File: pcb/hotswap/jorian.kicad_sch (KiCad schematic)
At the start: 59 parts, among them J1 USB-C Conn, J2 Ex_Bat, Q1 AO3407, SW1 SW_PUSH, SW10 SW_PUSH, SW11 SW_PUSH, SW12 SW_PUSH, SW13 SW_PUSH, SW14 SW_PUSH, SW15 SW_PUSH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

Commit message: Proper library management
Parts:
- D1, D3: footprint skean:LED_0603_1608Metric_REV -> kbd:LED_0603_1608Metric_REV
- D2: footprint skean:D_SOD-323_HandSoldering_REV -> kbd:D_SOD-323_HandSoldering_REV
- E10, E15, E16, E18, E19, E20, E21, E5: footprint kbd_jorian:edge_conn -> jorian:edge_conn
- G1, G2: footprint kbd:jorian_logo -> jorian:jorian_logo_840
- J1: footprint skean:USB-C_C168688_REV -> kbd:USB-C_C168688_REV
- J2: footprint skean:Battery_TH -> kbd:Battery_TH
- Q1: footprint skean:SOT-23_Handsoldering_REV -> kbd:SOT-23_Handsoldering_REV
- R1, R2, R3, R4, R5, R6, R7, R8: footprint skean:R_0603_1608Metric_REV -> kbd:R_0603_1608Metric_REV
- RSW1: footprint skean:SW_SPST_EVQP7C_REV -> kbd:SW_SPST_EVQP7C_REV
- SW23, SW24: footprint skean:SW_SPDT+H-MSK12C01_hor(7pin_SMD)_REV -> kbd:SW_SPDT+H-MSK12C01_hor(7pin_SMD)_REV
- U2, U3: footprint skean:SOT-23-5_HandSoldering_REV -> kbd:SOT-23-5_HandSoldering_REV

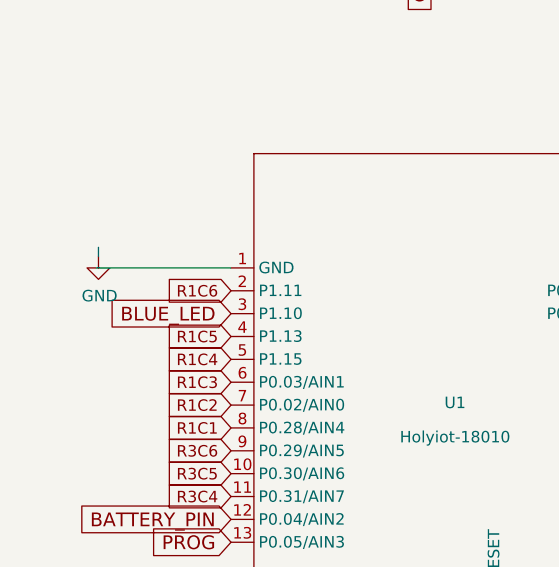
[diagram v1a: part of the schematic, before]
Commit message: Schematic ground fix
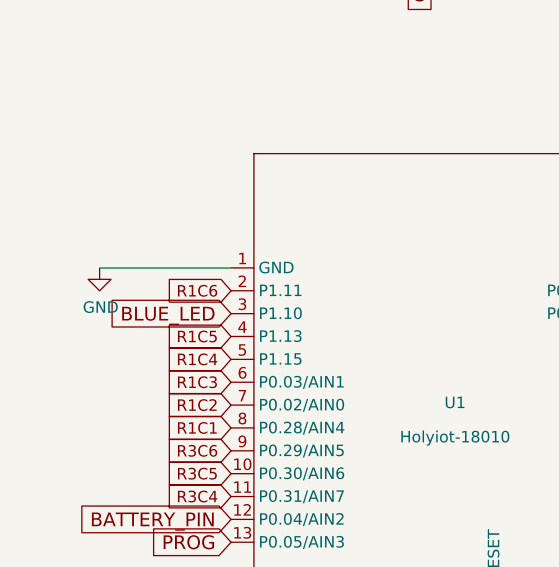
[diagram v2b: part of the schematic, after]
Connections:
- net GND: now also U1.1 (GND)
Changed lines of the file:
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@@
     (stroke (width 0) (type solid) (color 0 0 0 0))
+  )
+  (wire (pts (xy 19.05 105.41) (xy 33.655 105.41))
+    (stroke (width 0) (type default) (color 0 0 0 0))
   )
   (wire (pts (xy 81.915 105.41) (xy 90.043 105.41))
@@
     (stroke (width 0) (type solid) (color 0 0 0 0))
   )
-  (wire (pts (xy 18.923 103.124) (xy 18.923 104.14))
-    (stroke (width 0) (type solid) (color 0 0 0 0))
-  )
   (wire (pts (xy 78.74 189.865) (xy 80.01 189.865))
-    (stroke (width 0) (type solid) (color 0 0 0 0))
-  )
-  (wire (pts (xy 33.655 105.41) (xy 18.669 105.41))
     (stroke (width 0) (type solid) (color 0 0 0 0))
   )
@@
     )
   )
-  (symbol (lib_id "power:GND") (at 18.923 104.14 0) (unit 1)
-    (in_bom yes) (on_board yes)
-    (property "Reference" "#PWR021" (id 0) (at 18.923 110.49 0)
-      (effects (font (size 1.27 1.27)) hide)
-    )
-    (property "Value" "GND" (id 1) (at 19.05 108.5342 0))
-    (property "Footprint" "" (id 2) (at 18.923 104.14 0)
-      (effects (font (size 1.27 1.27)) hide)
-    )
-    (property "Datasheet" "" (id 3) (at 18.923 104.14 0)
-      (effects (font (size 1.27 1.27)) hide)
-    )
+  (symbol (lib_id "power:GND") (at 19.05 105.41 0) (unit 1)
+    (in_bom yes) (on_board yes)
+    (property "Reference" "#PWR021" (id 0) (at 19.05 111.76 0)
+      (effects (font (size 1.27 1.27)) hide)
+    )
+    (property "Value" "GND" (id 1) (at 19.177 109.8042 0))
+    (property "Footprint" "" (id 2) (at 19.05 105.41 0)
+      (effects (font (size 1.27 1.27)) hide)
+    )
+    (property "Datasheet" "" (id 3) (at 19.05 105.41 0)
+      (effects (font (size 1.27 1.27)) hide)
+    )
